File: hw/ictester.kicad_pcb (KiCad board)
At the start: 4 copper layers, 78.2 x 91.4 mm, 70 parts, among them J1 Conn_01x12_Pin, J2 Conn_01x12_Pin, J3 Conn_01x01_Pin, J4 Conn_01x01_Pin, J6 Conn_01x06_Pin, J7 Conn_01x04_Pin, J8 Conn_02x05_Odd_Even, J9 USB_B_Micro, U1 ATmega1284-A, U2 CP2102N-Axx-xQFN28, U3 CDSOT236-0504C, U4 MAX14662, U5 MAX14662, U6 MAX14662, U7 MAX14662, U8 MAX14662, U9 ZIF24, Y1 20MHz

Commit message: h/w update
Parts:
- added C18: 100n, Capacitor_SMD:C_0805_2012Metric_Pad1.18x1.45mm_HandSolder, F.Cu at (152.4, 75.7)
- C7: value 10n -> 100n
- moved C6 14.7 mm to (148.1, 62.0), turned to 180 degrees
- moved C8 1.27 mm to (170.2, 73.2)
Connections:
- U1 pad 29: +5V -> unconnected-(U1-AREF-Pad29)
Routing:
- net +5V: track 141.9 -> 126.3 mm, vias 41 -> 43
- net ~{RESET}: track 188.0 -> 182.5 mm
- net SCL1: track 87.4 -> 89.4 mm
- net GND: track 158.3 -> 160.1 mm, vias 24 -> 25

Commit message: hw update
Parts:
- C8: value C_Polarized -> 10u
- LED1: value Value: Inolux_IN-PI554FCH -> Inolux_IN-PI554FCH
- moved C2 9.72 mm to (132.1, 60.2), turned to -90 degrees
- moved C4 7.41 mm to (134.4, 60.2), turned to -90 degrees
- moved Y1 6.75 mm to (140.2, 60.4)
- moved C6 1.48 mm to (147.3, 60.7), turned to -90 degrees
- moved J9 0.08 mm to (177.1, 67.3)
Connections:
- net MISO renamed ZIF23
- net MOSI renamed ZIF22
- net SCK renamed ZIF24
- C1 pad 1: Net-(U2-VDD) -> Net-(J6-Pin_6)
- J6 pad 6: unconnected-(J6-Pin_6-Pad6) -> Net-(J6-Pin_6)
- J8 pad 4: GND -> +5V
- J8 pad 6: GND -> +5V
- U2 pad 6: Net-(U2-VDD) -> Net-(J6-Pin_6)
- U4 pad 10: (no net) -> unconnected-(U4-NC-Pad10)
- U4 pad 12: (no net) -> unconnected-(U4-NC-Pad12)
- U4 pad 13: (no net) -> unconnected-(U4-NC-Pad13)
- U5 pad 10: (no net) -> unconnected-(U5-NC-Pad10)
- U5 pad 12: (no net) -> unconnected-(U5-NC-Pad12)
- U5 pad 13: (no net) -> unconnected-(U5-NC-Pad13)
- U6 pad 10: (no net) -> unconnected-(U6-NC-Pad10)
- U6 pad 12: (no net) -> unconnected-(U6-NC-Pad12)
- U6 pad 13: (no net) -> unconnected-(U6-NC-Pad13)
- U7 pad 10: (no net) -> unconnected-(U7-NC-Pad10)
- U7 pad 12: (no net) -> unconnected-(U7-NC-Pad12)
- U7 pad 13: (no net) -> unconnected-(U7-NC-Pad13)
- U8 pad 10: (no net) -> unconnected-(U8-NC-Pad10)
- U8 pad 12: (no net) -> unconnected-(U8-NC-Pad12)
- U8 pad 13: (no net) -> unconnected-(U8-NC-Pad13)
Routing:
- net GND: track 160.1 -> 127.0 mm, vias 25 -> 31
- net Net-(J6-Pin_6): track 0.00 -> 16.7 mm, vias 0 -> 1
- net ZIF23: track 87.7 -> 95.3 mm
- net Net-(U2-VDD): track 6.57 -> 0.00 mm
- net Net-(U1-XTAL2): track 13.9 -> 16.1 mm
- net +5V: track 126.3 -> 128.3 mm
- net ZIF12: track 70.5 -> 68.6 mm
- net Net-(U1-XTAL1): track 15.3 -> 13.3 mm
- net ZIF11: track 70.8 -> 68.9 mm
- net ZIF10: track 72.0 -> 70.3 mm
- net ZIF9: track 55.9 -> 54.3 mm
- net ZIF14: track 76.4 -> 77.2 mm
- net ZIF15: track 76.7 -> 77.5 mm
- net ZIF16: track 59.7 -> 60.5 mm
- net ZIF13: track 74.8 -> 75.6 mm
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- added copper zone on F.Cu, net GND

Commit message: hw update
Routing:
- net +5VD: track 87.7 -> 89.8 mm
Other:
- board text added: "WayWayWay"

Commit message: H/W v3
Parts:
- removed H1, H2, H3, H4: MountingHole_Pad, MountingHole:MountingHole_3.2mm_M3_DIN965_Pad_TopBottom
- removed J8: Conn_02x05_Odd_Even, Connector_PinHeader_2.54mm:PinHeader_2x05_P2.54mm_Vertical
- removed J9: USB_B_Micro, Connector_USB:USB_Micro-B_Amphenol_10104110_Horizontal
- removed JP1: Jumper_2_Open, Connector_PinHeader_2.54mm:PinHeader_1x02_P2.54mm_Vertical
- added C19: 100n, Capacitor_SMD:C_0805_2012Metric_Pad1.18x1.45mm_HandSolder, F.Cu at (176.5, 64.5)
- added C20: 100n, Capacitor_SMD:C_0805_2012Metric_Pad1.18x1.45mm_HandSolder, B.Cu at (176.8, 84.2)
- added C21: 1u, Capacitor_SMD:C_0805_2012Metric_Pad1.18x1.45mm_HandSolder, B.Cu at (186.9, 107.9)
- added C22: 1u, Capacitor_SMD:C_0805_2012Metric_Pad1.18x1.45mm_HandSolder, B.Cu at (132.8, 117.2)
- added C23: 100n, Capacitor_SMD:C_0805_2012Metric_Pad1.18x1.45mm_HandSolder, B.Cu at (174.2, 88.4)
- added C24: 100n, Capacitor_SMD:C_0805_2012Metric_Pad1.18x1.45mm_HandSolder, B.Cu at (147.9, 101.8)
- added C25: 100n, Capacitor_SMD:C_0805_2012Metric_Pad1.18x1.45mm_HandSolder, B.Cu at (171.1, 93.5)
- added C26: 100n, Capacitor_SMD:C_0805_2012Metric_Pad1.18x1.45mm_HandSolder, B.Cu at (152.3, 100.2)
- added D1: RED, LED_SMD:LED_0805_2012Metric_Pad1.15x1.40mm_HandSolder, F.Cu at (184.9, 62.1)
- added D2: ORANGE, LED_SMD:LED_0805_2012Metric_Pad1.15x1.40mm_HandSolder, F.Cu at (153.8, 66.2)
- added J5: Conn_02x05_Odd_Even, Connector_PinHeader_2.54mm:PinHeader_2x05_P2.54mm_Vertical, F.Cu at (149.9, 62.2)
- added R30: 4k7, Resistor_SMD:R_0805_2012Metric_Pad1.20x1.40mm_HandSolder, F.Cu at (182.6, 62.1)
- added R31: 133k, Resistor_SMD:R_0805_2012Metric_Pad1.20x1.40mm_HandSolder, B.Cu at (187.5, 83.2)
- added R32: 1k0, Resistor_SMD:R_0805_2012Metric_Pad1.20x1.40mm_HandSolder, F.Cu at (187.3, 62.1)
- added R33: 200m, Resistor_SMD:R_0805_2012Metric_Pad1.20x1.40mm_HandSolder, B.Cu at (183.2, 88.5)
- added R34: 200m, Resistor_SMD:R_0805_2012Metric_Pad1.20x1.40mm_HandSolder, B.Cu at (147.8, 93.6)
- added R35: 47, Resistor_SMD:R_0805_2012Metric_Pad1.20x1.40mm_HandSolder, B.Cu at (178.7, 87.5)
- added R36: 47, Resistor_SMD:R_0805_2012Metric_Pad1.20x1.40mm_HandSolder, B.Cu at (178.7, 89.5)
- added R37: 47, Resistor_SMD:R_0805_2012Metric_Pad1.20x1.40mm_HandSolder, B.Cu at (146.5, 98.5)
- added R38: 47, Resistor_SMD:R_0805_2012Metric_Pad1.20x1.40mm_HandSolder, B.Cu at (149.1, 98.5)
- added R39: 1k0, Resistor_SMD:R_0805_2012Metric_Pad1.20x1.40mm_HandSolder, F.Cu at (156.0, 66.2)
- added R40: 4k7, Resistor_SMD:R_0805_2012Metric_Pad1.20x1.40mm_HandSolder, B.Cu at (161.3, 86.5)
- added R41: 0, Resistor_SMD:R_0805_2012Metric_Pad1.20x1.40mm_HandSolder, B.Cu at (187.5, 85.5)
- added RN1: 120, Resistor_SMD:R_Array_Convex_4x0603, F.Cu at (163.1, 90.6)
- added RN10: 1M, Resistor_SMD:R_Array_Convex_4x0603, F.Cu at (142.5, 78.7)
- added RN11: 120, Resistor_SMD:R_Array_Convex_4x0603, F.Cu at (144.4, 89.6)
- added RN12: 1M, Resistor_SMD:R_Array_Convex_4x0603, F.Cu at (136.9, 84.7)
- added RN2: 1M, Resistor_SMD:R_Array_Convex_4x0603, F.Cu at (180.6, 127.6)
- added RN3: 120, Resistor_SMD:R_Array_Convex_4x0603, F.Cu at (157.2, 90.5)
- added RN4: 1M, Resistor_SMD:R_Array_Convex_4x0603, F.Cu at (138.9, 127.6)
- added RN5: 120, Resistor_SMD:R_Array_Convex_4x0603, F.Cu at (172.8, 88.8)
- added RN6: 1M, Resistor_SMD:R_Array_Convex_4x0603, F.Cu at (173.6, 95.4)
- added RN7: 120, Resistor_SMD:R_Array_Convex_4x0603, F.Cu at (174.4, 83.7)
- added RN8: 1M, Resistor_SMD:R_Array_Convex_4x0603, F.Cu at (173.6, 99.3)
- added RN9: 120, Resistor_SMD:R_Array_Convex_4x0603, F.Cu at (148.1, 77.7)
- added U10: CP2102N, Package_DFN_QFN:QFN-28-1EP_5x5mm_P0.5mm_EP3.35x3.35mm, F.Cu at (169.4, 61.6)
- added U11: TPS2553, Package_TO_SOT_SMD:SOT-23-6_Handsoldering, B.Cu at (181.8, 83.2)
- added U12: INA236, Package_TO_SOT_SMD:SOT-23-8_Handsoldering, B.Cu at (169.6, 89.0)
- added U13: INA236, Package_TO_SOT_SMD:SOT-23-8_Handsoldering, B.Cu at (148.5, 106.2)
- C1, R10, R11, R12, R13, R14, R15, R16, R17, R18, R19, R2, R20, R21, R22, R23, R24, R26, R27, R28, R29, R3, R4, R5, R6, R7, R8, R9, U5, U6: moved to B.Cu
- C10, C11: value 100n -> 22p
- C15, C17: value 470p -> 100n
- C16: value 470p -> 1u
- C18: value 100n -> 10u; footprint Capacitor_SMD:C_0805_2012Metric_Pad1.18x1.45mm_HandSolder -> Capacitor_Tantalum_SMD:CP_EIA-3528-21_Kemet-B_Pad1.50x2.35mm_HandSolder
- C2, C4: value 22p -> 100n; moved to B.Cu
- C3, C6, C7: value 100n -> 470p; moved to B.Cu
- C5: value 1u -> 100p; moved to B.Cu
- C8: value 10u -> 100n; footprint Capacitor_Tantalum_SMD:CP_EIA-3528-21_Kemet-B_Pad1.50x2.35mm_HandSolder -> Capacitor_SMD:C_0805_2012Metric_Pad1.18x1.45mm_HandSolder; moved to B.Cu
- C9: value 470p -> 100n; moved to B.Cu
- J1: value Conn_01x12_Pin -> Conn_01x01_Pin; footprint Connector_PinHeader_2.54mm:PinHeader_1x12_P2.54mm_Vertical -> Connector_PinHeader_2.54mm:PinHeader_1x01_P2.54mm_Vertical
- J3: value Conn_01x01_Pin -> Conn_01x12_Pin; footprint Connector_PinHeader_2.54mm:PinHeader_1x01_P2.54mm_Vertical -> Connector_PinHeader_2.54mm:PinHeader_1x12_P2.54mm_Vertical
- J6: value Conn_01x06_Pin -> USB_B_Micro; footprint Connector_PinHeader_2.54mm:PinHeader_1x06_P2.54mm_Vertical -> Connector_USB:USB_Micro-B_Amphenol_10118193-0001LF_Horizontal
- J7: value Conn_01x04_Pin -> Conn_02x01; footprint Connector_PinHeader_2.54mm:PinHeader_1x04_P2.54mm_Vertical -> Connector_PinHeader_2.54mm:PinHeader_1x02_P2.54mm_Vertical
- R1: value 10k -> 4k7; moved to B.Cu
- R25: value 4k7 -> 10k
- U1: value ATmega1284-A -> MAX14662; footprint Package_QFP:TQFP-44_10x10mm_P0.8mm -> Package_DFN_QFN:QFN-28-1EP_4x4mm_P0.4mm_EP2.6x2.6mm; moved to B.Cu
- U2: value CP2102N-Axx-xQFN28 -> MAX14662; footprint Package_DFN_QFN:QFN-28-1EP_5x5mm_P0.5mm_EP3.35x3.35mm -> Package_DFN_QFN:QFN-28-1EP_4x4mm_P0.4mm_EP2.6x2.6mm; moved to B.Cu
- U3: value CDSOT236-0504C -> MAX14662; footprint Package_TO_SOT_SMD:SOT-23-6 -> Package_DFN_QFN:QFN-28-1EP_4x4mm_P0.4mm_EP2.6x2.6mm; moved to B.Cu
- U4: value MAX14662 -> ZIF24; footprint Package_DFN_QFN:QFN-28-1EP_4x4mm_P0.4mm_EP2.6x2.6mm -> Socket:DIP_Socket-24_W11.9_W12.7_W15.24_W17.78_W18.5_3M_224-1275-00-0602J
- U7: value MAX14662 -> 74LVC1G07; footprint Package_DFN_QFN:QFN-28-1EP_4x4mm_P0.4mm_EP2.6x2.6mm -> Package_TO_SOT_SMD:SOT-23-5_HandSoldering
- U8: value MAX14662 -> ATmega1284-A; footprint Package_DFN_QFN:QFN-28-1EP_4x4mm_P0.4mm_EP2.6x2.6mm -> Package_QFP:TQFP-44_10x10mm_P0.8mm
- U9: value ZIF24 -> USBLC6-2SC6; footprint Socket:DIP_Socket-24_W11.9_W12.7_W15.24_W17.78_W18.5_3M_224-1275-00-0602J -> Package_TO_SOT_SMD:SOT-23-6
- moved C10 75.9 mm to (164.0, 65.8), turned to 45 degrees
- moved R3 74.8 mm to (186.9, 118.0)
- moved R2 73.9 mm to (186.9, 113.3), turned to 0 degrees
- moved C2 72.7 mm to (155.3, 129.1)
- moved C14 67.0 mm to (171.8, 76.2), turned to -135 degrees
- moved J1 66.6 mm to (175.3, 137.2)
- moved J7 66.2 mm to (179.6, 79.1), turned to -90 degrees
- moved R10 65.3 mm to (162.7, 135.9), turned to -90 degrees
- moved R9 65.0 mm to (160.5, 135.9), turned to -90 degrees
- moved R7 64.8 mm to (156.1, 136.0), turned to -90 degrees
- moved R8 64.8 mm to (158.3, 136.0), turned to -90 degrees
- moved R6 64.4 mm to (153.0, 136.0), turned to -90 degrees
- moved U2 61.1 mm to (159.4, 127.8), turned to -90 degrees
- moved R12 60.5 mm to (167.0, 135.9), turned to -90 degrees
- moved R11 60.4 mm to (164.8, 136.0), turned to -90 degrees
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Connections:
- C1 pad 1: Net-(J6-Pin_6) -> +5V
- C10 pad 1: +5V -> Net-(U8-XTAL1)
- C11 pad 1: +5V -> GND
- C11 pad 2: GND -> Net-(U8-XTAL2)
- C12 pad 1: +5V -> GND
- C12 pad 2: GND -> +5V
- C13 pad 1: +5V -> GND
- C13 pad 2: GND -> +5V
- C14 pad 1: +5V -> GND
- C14 pad 2: GND -> +5V
- C15 pad 1: Net-(U8-B5) -> +5V
- C15 pad 2: Net-(U8-B4) -> GND
- C16 pad 1: Net-(U8-B8) -> +5V
- C16 pad 2: Net-(U8-B4) -> GND
- C17 pad 1: Net-(U7-A7) -> +5V
- C17 pad 2: Net-(U7-A8) -> GND
- C18 pad 1: GND -> +5V
- C18 pad 2: +5V -> GND
- C2 pad 1: GND -> +5V
- C2 pad 2: Net-(U1-XTAL1) -> GND
- C3 pad 1: +5V -> Net-(U3-A7)
- C3 pad 2: GND -> Net-(U3-A8)
- C4 pad 1: GND -> +5V
- C4 pad 2: Net-(U1-XTAL2) -> GND
- C5 pad 1: +5V -> GND
- C5 pad 2: GND -> Net-(U3-B2)
- C6 pad 1: GND -> Net-(U3-B1)
- C6 pad 2: +5V -> Net-(U3-B2)
- C7 pad 1: GND -> Net-(U3-B5)
- C7 pad 2: +5V -> Net-(U3-B6)
- C9 pad 1: Net-(U5-B6) -> +5V
- C9 pad 2: Net-(U5-B7) -> GND
- J1 pad 1: ZIF1 -> GND
- J3 pad 1: GND -> ZIF1
- J6 pad 2: GND -> Net-(J6-D-)
- J6 pad 3: TXD -> Net-(J6-D+)
- J6 pad 4: RXD -> unconnected-(J6-ID-Pad4)
- J6 pad 5: unconnected-(J6-Pin_5-Pad5) -> GND
- J6 pad 6: Net-(J6-Pin_6) -> GND
- J7 pad 1: +5V -> Net-(J7-Pin_1)
- J7 pad 2: Net-(J7-Pin_2) -> +5V
- R1 pad 1: +5V -> Net-(U1-A3)
- R1 pad 2: ~{RESET} -> +5V
- R10 pad 1: Net-(U4-A7) -> Net-(U2-B6)
- R11 pad 1: Net-(U5-B8) -> Net-(U2-B7)
- R12 pad 1: Net-(U5-B6) -> Net-(U2-B8)
- R13 pad 1: Net-(U5-B2) -> +5V
- R13 pad 2: +5V -> Net-(U3-B1)
- R14 pad 1: Net-(U5-B1) -> +5V
- R14 pad 2: +5V -> Net-(U3-B3)
- R15 pad 1: Net-(U6-A2) -> +5V
- R15 pad 2: +5V -> Net-(U3-B5)
- R16 pad 1: Net-(U6-A3) -> Net-(U5-B3)
- R17 pad 1: Net-(U6-A5) -> Net-(U5-B5)
- R18 pad 1: Net-(U6-A6) -> Net-(U5-B7)
- R19 pad 1: Net-(U6-A7) -> Net-(U6-B1)
- R2 pad 1: +5V -> Net-(U1-A5)
- R2 pad 2: SDA1 -> +5V
- R20 pad 1: Net-(U6-A8) -> Net-(U6-B2)
- R21 pad 1: Net-(U8-B1) -> Net-(U6-B3)
- R22 pad 1: Net-(U8-B4) -> Net-(U6-B4)
- R23 pad 1: Net-(U8-B6) -> Net-(U6-B7)
- R24 pad 1: Net-(U7-A8) -> Net-(U6-B8)
- R25 pad 1: Net-(U7-A5) -> +5V
- R25 pad 2: +5V -> Net-(J5-Pin_5)
- R26 pad 1: Net-(U7-A4) -> +5V
- R26 pad 2: +5V -> SDA1
- R27 pad 1: Net-(U7-A3) -> +5V
- R27 pad 2: +5V -> SCL1
- R28 pad 1: Net-(U7-A2) -> +5V
- R28 pad 2: +5V -> SDA2
- R29 pad 1: Net-(U7-A1) -> +5V
- R29 pad 2: +5V -> SCL2
- R3 pad 1: +5V -> Net-(U1-A7)
- R3 pad 2: SCL1 -> +5V
- R4 pad 1: +5V -> Net-(U1-A8)
- R4 pad 2: SDA2 -> +5V
- R5 pad 1: +5V -> Net-(U3-A8)
- R5 pad 2: SCL2 -> +5V
- R6 pad 1: Net-(U4-A2) -> Net-(U2-B1)
- R7 pad 1: Net-(U4-A3) -> Net-(U2-B3)
- R8 pad 1: Net-(U4-A4) -> Net-(U2-B4)
- R9 pad 1: Net-(U4-A5) -> Net-(U2-B5)
- U1 pad 1: ZIF22 -> GND
- U1 pad 10: RXD -> unconnected-(U1-NC-Pad10)
- U1 pad 11: Net-(LED1-DIN) -> GND
- U1 pad 12: SDA1 -> unconnected-(U1-NC-Pad12)
- U1 pad 13: SCL1 -> unconnected-(U1-NC-Pad13)
- U1 pad 14: SDA2 -> ZIF18
- U1 pad 15: SCL2 -> ZIF19
- U1 pad 16: Net-(J7-Pin_2) -> ZIF20
- U1 pad 17: +5V -> ZIF20
- U1 pad 18: GND -> ZIF21
- U1 pad 19: ZIF1 -> ZIF24
- U1 pad 2: ZIF23 -> GNDUT
- U1 pad 20: ZIF2 -> ZIF24
- U1 pad 21: ZIF3 -> ZIF24
- U1 pad 22: ZIF4 -> ~{SD}
- U1 pad 23: ZIF5 -> GND
- U1 pad 24: ZIF6 -> SCL2
- U1 pad 25: ZIF7 -> GND
- U1 pad 26: ZIF8 -> +5V
- U1 pad 27: +5V -> SDA2
- U1 pad 29: unconnected-(U1-AREF-Pad29) -> GND
- U1 pad 3: ZIF24 -> VDUT
- U1 pad 4: ~{RESET} -> Net-(U1-A3)
- U1 pad 5: +5V -> GNDUT
- U1 pad 6: GND -> Net-(U1-A5)
- U1 pad 7: Net-(U1-XTAL2) -> GNDUT
- U1 pad 8: Net-(U1-XTAL1) -> Net-(U1-A7)
- U1 pad 9: TXD -> Net-(U1-A8)
- U2 pad 1: unconnected-(U2-~{DCD}-Pad1) -> GND
- U2 pad 11: unconnected-(U2-~{SUSPEND}-Pad11) -> GND
- U2 pad 14: unconnected-(U2-CHR1-Pad14) -> Net-(U2-B8)
- U2 pad 15: unconnected-(U2-CHR0-Pad15) -> Net-(U2-B7)
- U2 pad 16: unconnected-(U2-~{WAKEUP}/GPIO.3-Pad16) -> Net-(U2-B6)
- U2 pad 17: unconnected-(U2-RS485/GPIO.2-Pad17) -> Net-(U2-B5)
- U2 pad 18: unconnected-(U2-~{RXT}/GPIO.1-Pad18) -> Net-(U2-B4)
- U2 pad 19: unconnected-(U2-~{TXT}/GPIO.0-Pad19) -> Net-(U2-B3)
- U2 pad 2: unconnected-(U2-~{RI}/CLK-Pad2) -> ZIF12
- U2 pad 20: unconnected-(U2-GPIO.6-Pad20) -> GNDUT
- U2 pad 21: unconnected-(U2-GPIO.5-Pad21) -> Net-(U2-B1)
- U2 pad 22: unconnected-(U2-GPIO.4-Pad22) -> ~{SD}
- U2 pad 23: unconnected-(U2-~{CTS}-Pad23) -> GND
- U2 pad 24: unconnected-(U2-~{RTS}-Pad24) -> SCL1
- U2 pad 25: RXD -> GND
- U2 pad 26: TXD -> +5V
- U2 pad 27: unconnected-(U2-~{DSR}-Pad27) -> SDA1
- U2 pad 28: unconnected-(U2-~{DTR}-Pad28) -> +5V
- U2 pad 3: GND -> ZIF12
- U2 pad 4: Net-(J9-D+) -> ZIF11
- U2 pad 5: Net-(J9-D-) -> ZIF17
- U2 pad 6: Net-(J6-Pin_6) -> ZIF16
- U2 pad 7: +5V -> ZIF15
- U2 pad 8: +5V -> ZIF14
- U2 pad 9: ~{RESET} -> ZIF13
- U3 pad 1: unconnected-(U3-IO1-Pad1) -> GND
- U3 pad 2: GND -> ZIF23
- U3 pad 3: Net-(J9-D-) -> ZIF22
- U3 pad 4: Net-(J9-D+) -> ZIF22
- U3 pad 5: +5V -> ZIF21
- U3 pad 6: unconnected-(U3-IO4-Pad6) -> ZIF21
- U4 pad 1: GND -> ZIF1
- U4 pad 10: unconnected-(U4-NC-Pad10) -> ZIF10
- U4 pad 11: GND -> ZIF11
- U4 pad 12: unconnected-(U4-NC-Pad12) -> ZIF12
- U4 pad 13: unconnected-(U4-NC-Pad13) -> ZIF13
- U4 pad 14: ZIF5 -> ZIF14
- U4 pad 15: ZIF5 -> ZIF15
- U4 pad 16: ZIF4 -> ZIF16
- U4 pad 17: ZIF4 -> ZIF17
- U4 pad 18: ZIF3 -> ZIF18
- U4 pad 19: ZIF2 -> ZIF19
- U4 pad 2: GND -> ZIF2
- U4 pad 20: ZIF1 -> ZIF20
- U4 pad 21: ZIF1 -> ZIF21
- U4 pad 22: ~{RESET} -> ZIF22
- U4 pad 23: GND -> ZIF23
- U4 pad 24: SCL1 -> ZIF24
- U4 pad 3: Net-(U4-A2) -> ZIF3
- U4 pad 4: Net-(U4-A3) -> ZIF4
- U4 pad 5: Net-(U4-A4) -> ZIF5
- U4 pad 6: Net-(U4-A5) -> ZIF6
- U4 pad 7: +5VD -> ZIF7
- U4 pad 8: Net-(U4-A7) -> ZIF8
- U4 pad 9: +5VD -> ZIF9
- U5 pad 14: Net-(U5-B8) -> GNDUT
- U5 pad 16: Net-(U5-B6) -> VDUT
- U5 pad 17: GND -> Net-(U5-B5)
- U5 pad 18: GND -> GNDUT
- U5 pad 19: +5VD -> Net-(U5-B3)
- U5 pad 2: ZIF9 -> ZIF7
- U5 pad 20: Net-(U5-B2) -> VDUT
- U5 pad 21: Net-(U5-B1) -> GNDUT
- U5 pad 22: ~{RESET} -> ~{SD}
- U5 pad 6: ZIF7 -> ZIF9
- U5 pad 7: ZIF7 -> ZIF9
- U5 pad 8: ZIF6 -> ZIF10
- U5 pad 9: ZIF6 -> ZIF10
- U6 pad 14: ZIF13 -> Net-(U6-B8)
- U6 pad 15: ZIF14 -> Net-(U6-B7)
- U6 pad 16: ZIF15 -> VDUT
- U6 pad 17: ZIF10 -> VDUT
- U6 pad 18: ZIF10 -> Net-(U6-B4)
- U6 pad 19: ZIF11 -> Net-(U6-B3)
- U6 pad 2: GND -> ZIF1
- U6 pad 20: ZIF12 -> Net-(U6-B2)
- U6 pad 21: ZIF12 -> Net-(U6-B1)
- U6 pad 22: ~{RESET} -> ~{SD}
- U6 pad 28: +5V -> GND
- U6 pad 3: Net-(U6-A2) -> ZIF2
- U6 pad 4: Net-(U6-A3) -> ZIF3
- U6 pad 5: GND -> ZIF4
- U6 pad 6: Net-(U6-A5) -> ZIF4
- U6 pad 7: Net-(U6-A6) -> ZIF5
- U6 pad 8: Net-(U6-A7) -> ZIF5
- U6 pad 9: Net-(U6-A8) -> ZIF6
- U7 pad 1: GND -> unconnected-(U7-NC-Pad1)
- U7 pad 2: Net-(U7-A1) -> Net-(J5-Pin_5)
- U7 pad 3: Net-(U7-A2) -> GND
- U7 pad 4: Net-(U7-A3) -> ~{SD}
- U7 pad 5: Net-(U7-A4) -> +5V
- U8 pad 1: GND -> Net-(J5-Pin_1)
- U8 pad 10: unconnected-(U8-NC-Pad10) -> USB_RXD
- U8 pad 11: GND -> Net-(LED1-DIN)
- U8 pad 12: unconnected-(U8-NC-Pad12) -> SDA1
- U8 pad 13: unconnected-(U8-NC-Pad13) -> SCL1
- U8 pad 14: Net-(U8-B8) -> SDA2
- U8 pad 15: GND -> SCL2
- U8 pad 16: Net-(U8-B6) -> VDUT_EN
- U8 pad 17: Net-(U8-B5) -> +5V
- U8 pad 18: Net-(U8-B4) -> GND
- U8 pad 19: GND -> Net-(RN9-R1.2)
- U8 pad 2: ZIF24 -> Net-(J5-Pin_9)
- U8 pad 20: +5VD -> Net-(RN9-R2.2)
- U8 pad 21: Net-(U8-B1) -> Net-(RN9-R3.2)
- U8 pad 22: ~{RESET} -> Net-(RN9-R4.2)
- U8 pad 23: GND -> Net-(RN11-R1.2)
- U8 pad 24: SCL2 -> Net-(RN11-R2.2)
- U8 pad 25: GND -> Net-(RN11-R3.2)
- U8 pad 26: +5V -> Net-(RN11-R4.2)
- U8 pad 27: SDA2 -> +5V
- U8 pad 29: GND -> unconnected-(U8-AREF-Pad29)
- U8 pad 3: ZIF24 -> Net-(J5-Pin_7)
- U8 pad 4: ZIF24 -> Net-(J5-Pin_5)
- U8 pad 5: ZIF23 -> +5V
- U8 pad 6: ZIF22 -> GND
- U8 pad 7: ZIF22 -> Net-(U8-XTAL2)
- U8 pad 8: ZIF21 -> Net-(U8-XTAL1)
- U8 pad 9: ZIF21 -> USB_TXD
- U9 pad 1: ZIF1 -> Net-(U10-D+)
- U9 pad 2: ZIF2 -> GND
- U9 pad 3: ZIF3 -> Net-(U10-D-)
- U9 pad 4: ZIF4 -> Net-(J6-D-)
- U9 pad 5: ZIF5 -> +5V
- U9 pad 6: ZIF6 -> Net-(J6-D+)
- Y1 pad 1: Net-(U1-XTAL2) -> Net-(U8-XTAL2)
- Y1 pad 3: Net-(U1-XTAL1) -> Net-(U8-XTAL1)
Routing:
- net ~{SD}: track 0.00 -> 198.1 mm, vias 0 -> 9
- net ~{RESET}: track 182.4 -> 0.00 mm, vias 6 -> 0
- net +5VD: track 89.8 -> 0.00 mm, vias 4 -> 0
- net GNDUT: track 0.00 -> 86.3 mm, vias 0 -> 11
- net ZIF23: track 95.3 -> 35.7 mm, vias 1 -> 2
- net ZIF24: track 87.8 -> 32.7 mm, vias 1 -> 0
- net VDUT: track 0.00 -> 51.4 mm, vias 0 -> 9
- net ZIF22: track 84.8 -> 39.5 mm, vias 1 -> 2
- net VDUT_EN: track 0.00 -> 35.7 mm, vias 0 -> 1
- net Net-(J5-Pin_1): track 0.00 -> 34.7 mm, vias 0 -> 1
- net TXD: track 32.0 -> 0.00 mm, vias 3 -> 0
- net RXD: track 31.4 -> 0.00 mm, vias 2 -> 0
- net SCL1: track 89.4 -> 120.1 mm, vias 3 -> 8
- net SDA1: track 95.8 -> 126.3 mm, vias 3 -> 7
- net Net-(J5-Pin_5): track 0.00 -> 29.8 mm, vias 0 -> 1
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- added copper zone on In1.Cu, net GNDUT
- added copper zone on In2.Cu, net VDUT
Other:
- board size 78.2 x 91.4 mm -> 66 x 90 mm
- board text added: "DEBUG"
- board text added: "Logic IC tester v3"
- board text removed: "DEBUG CONN"
- board text removed: "Logic IC tester"
- board text removed: "MISO"
- board text removed: "MOSI"
- board text removed: "NC"
- board text removed: "PD7 IO"
- board text removed: "SCK"
- board text removed: "https://mera400.pl"
- board text removed: "~{RESET}"

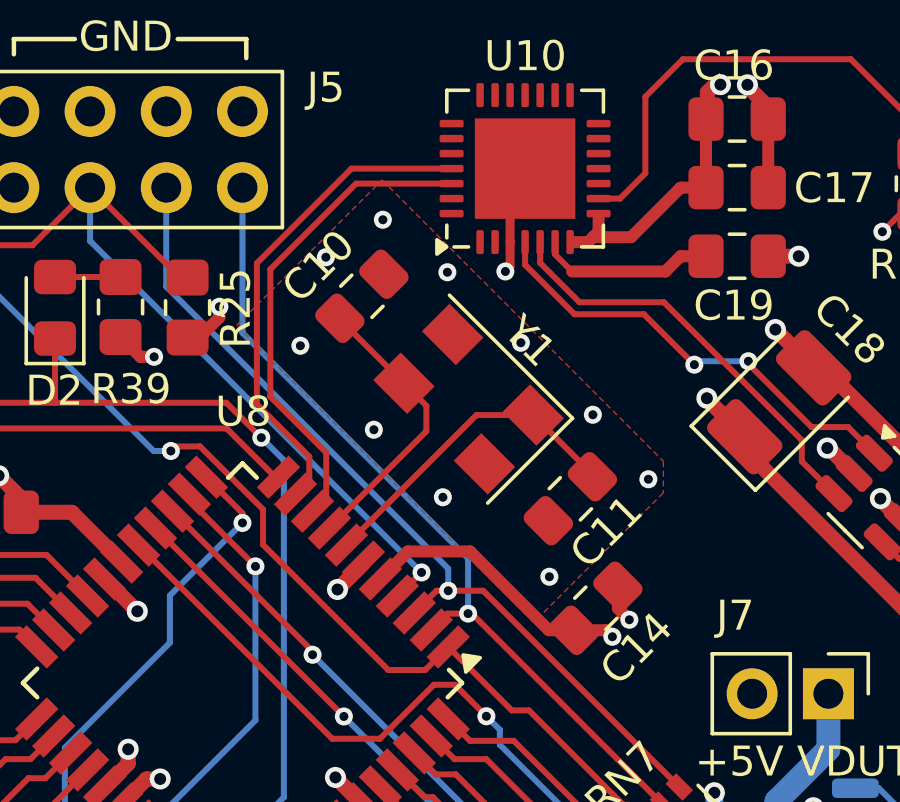
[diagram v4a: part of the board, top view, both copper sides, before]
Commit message: improve oscillator grounding
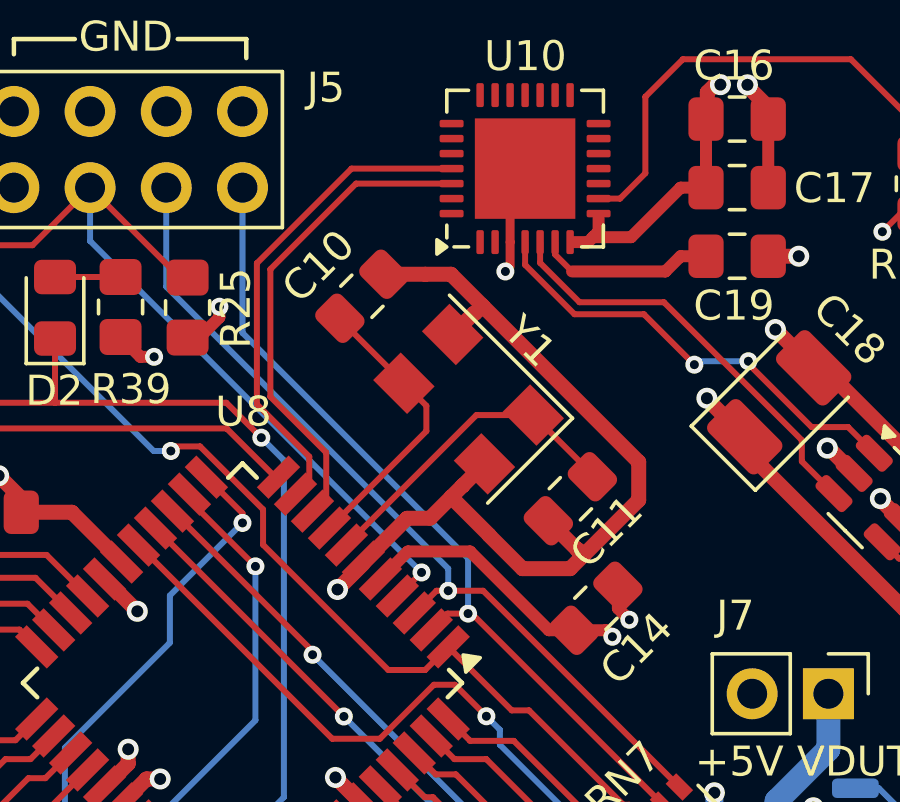
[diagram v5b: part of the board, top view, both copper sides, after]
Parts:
- added NT1: NetTie_2, NetTie:NetTie-2_SMD_Pad0.5mm, F.Cu at (166.6, 72.9)
- C5: value 100p -> 470p
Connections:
- C10 pad 2: GND -> /MCU/GNDOSC
- C11 pad 1: GND -> /MCU/GNDOSC
- Y1 pad 2: GND -> /MCU/GNDOSC
- Y1 pad 4: GND -> /MCU/GNDOSC
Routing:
- net /MCU/GNDOSC: track 0.00 -> 25.1 mm
- net GND: track 148.3 -> 151.2 mm, vias 59 -> 49
